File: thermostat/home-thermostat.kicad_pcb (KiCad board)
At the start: 2 copper layers, 92 parts, among them J1 Thermosthat, J2 Conn_01x24, J3 Conn_01x06, J4 AVR-ISP-6, Q1 BC817, Q2 BC817, Q3 BSS806NL6327, Q4 BC817, Q5 BSS806NL6327, Q6 BC817, Q7 BSS806NL6327, SW1 UP, SW2 DOWN, SW3 LEFT, SW4 RIGHT, SW5 OK, SW6 CANCEL, U1 ESP-12F, U2 MCP7940N-xMS, U3 LM2574M-5, U4 LD1117S33TR_SOT223, U5 AT24C512, U6 ATmega328P-AU, U7 LM358, U8 MCP9844, Y1 GEY KX-327NHT 12, Y2 20MHz ABM3B

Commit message: Started layouting thermosthat.
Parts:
- added Waveshare 4.2 Inch raw panel: waveshare_4.2_raw_panel, myfootprints:waveshare_4.2_raw_panel_folded_connector, B.Cu at (111.8, 135.9)
- moved C5 238.3 mm to (88.4, 168.9), turned to 270 degrees
- moved R4 223.3 mm to (86.6, 168.9), turned to 270 degrees
- moved U4 208.7 mm to (103.4, 102.9)
- moved C16 208.7 mm to (97.2, 105.2)
- moved C19 208.7 mm to (97.2, 102.9)
- moved U1 206.0 mm to (89.9, 156.7), turned to 90 degrees
- moved R3 203.4 mm to (90.4, 168.9), turned to 270 degrees
- moved C15 197.9 mm to (123.3, 119.5)
- moved C20 197.9 mm to (106.8, 110.4)
- moved D4 197.9 mm to (121.7, 111.9)
- moved L2 197.9 mm to (116.1, 110.4)
- moved U3 197.9 mm to (116.1, 119.3)
- moved R1 195.5 mm to (95.0, 144.8), turned to 270 degrees
- moved R5 189.2 mm to (98.0, 144.8), turned to 90 degrees
- moved C4 186.3 mm to (100.3, 169.2), turned to 270 degrees
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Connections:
- J3 pad 2: /DTR -> GND
- J3 pad 4: /RTC_INT -> /AVR_INT
- J3 pad 5: /AVR_INT -> /DTR
- J3 pad 6: GND -> /RTC_INT
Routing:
- net /GPIO0: track 0.00 -> 125.3 mm, vias 0 -> 2
- net GND: track 0.00 -> 87.8 mm, vias 0 -> 42
- net /GPIO15: track 0.00 -> 76.6 mm, vias 0 -> 2
- net /GPIO2: track 0.00 -> 76.1 mm, vias 0 -> 2
- net /SCK: track 0.00 -> 61.5 mm, vias 0 -> 2
- net /eink-RST: track 0.00 -> 61.3 mm, vias 0 -> 2
- net /MOSI: track 0.00 -> 58.1 mm, vias 0 -> 2
- net /SCL: track 0.00 -> 53.1 mm
- net /SDA: track 0.00 -> 50.5 mm
- net /nRST: track 0.00 -> 50.2 mm
- net +3V3: track 0.00 -> 33.2 mm, vias 0 -> 3
- net +5V: track 0.00 -> 30.1 mm, vias 0 -> 1
- net /PREVGL: track 0.00 -> 26.1 mm
- net /RESE: track 0.00 -> 24.6 mm
- net /PREVGH: track 0.00 -> 24.0 mm
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- added copper zone on B.Cu, net GND

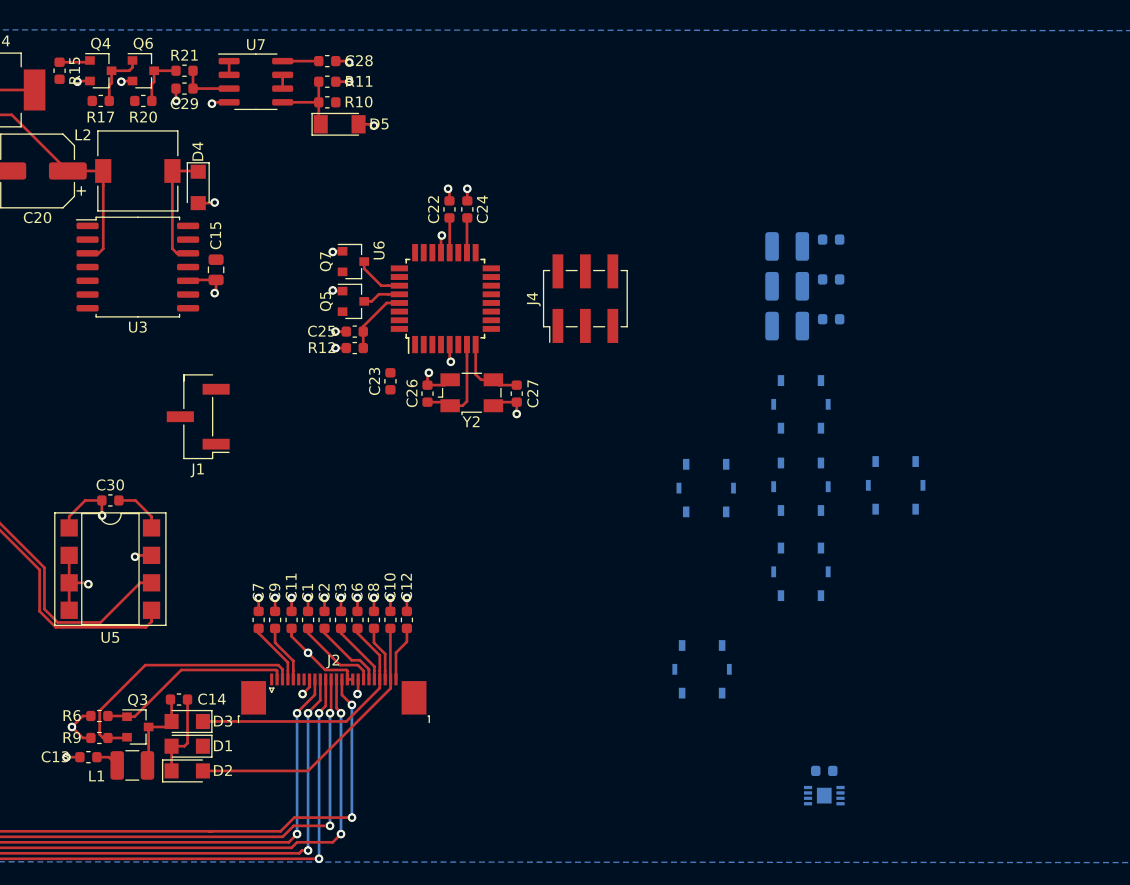
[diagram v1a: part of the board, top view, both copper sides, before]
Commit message: Advanced component placement, laid out some routes.
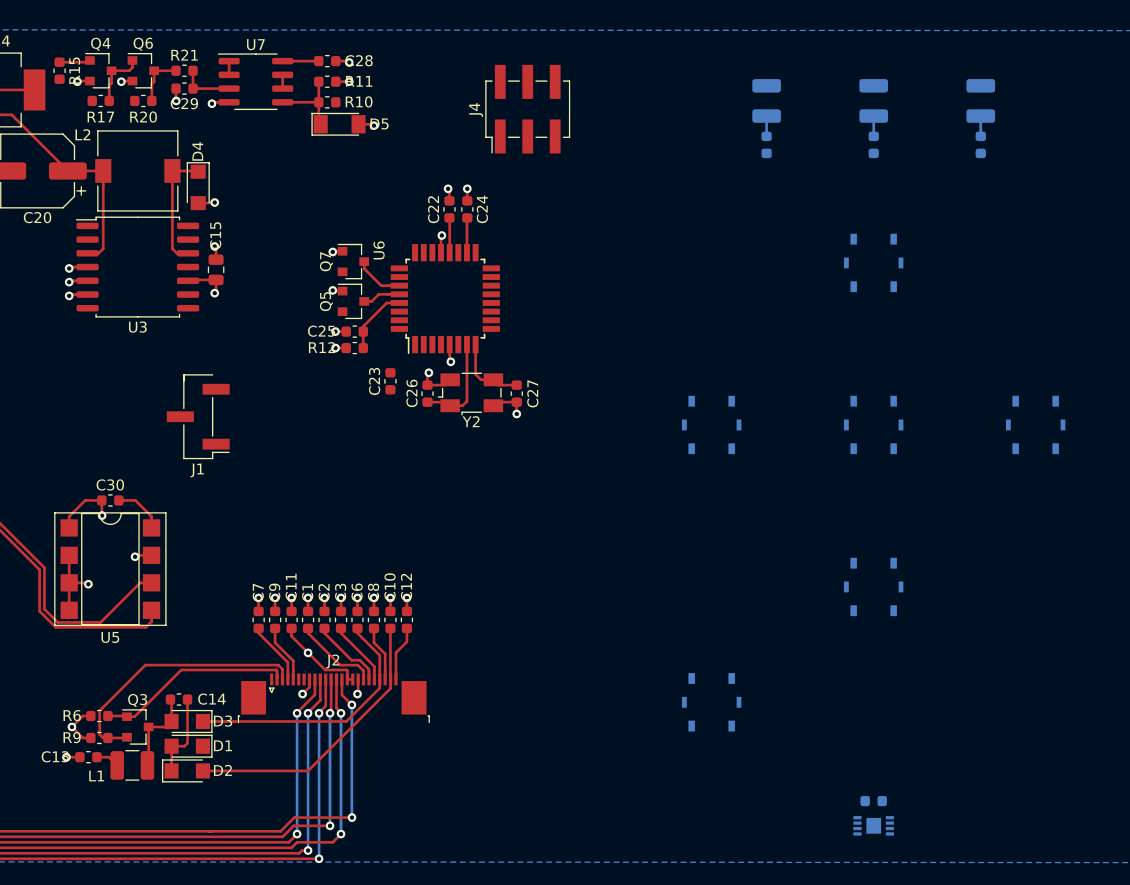
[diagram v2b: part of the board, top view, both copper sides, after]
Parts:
- moved D8 22.4 mm to (194.1, 103.9), turned to 270 degrees
- moved D7 20.9 mm to (174.2, 103.9), turned to 270 degrees
- moved D6 18.9 mm to (184.2, 103.9), turned to 270 degrees
- moved J4 18.3 mm to (152.1, 104.6)
- moved R14 17.2 mm to (174.2, 108.0), turned to 270 degrees
- moved R19 16.4 mm to (194.1, 108.0), turned to 270 degrees
- moved SW1 14.7 mm to (184.2, 118.9)
- moved SW3 14.1 mm to (199.1, 133.9)
- moved R13 13.1 mm to (184.2, 108.0), turned to 270 degrees
- moved SW5 8.83 mm to (184.2, 133.9)
- moved SW2 6.87 mm to (184.2, 148.8)
- moved SW4 5.86 mm to (169.2, 133.9)
- moved C21 5.36 mm to (184.2, 168.7)
- moved U8 5.36 mm to (184.2, 170.9)
- moved SW6 3.17 mm to (169.2, 159.5)
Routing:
- net GND: track 87.8 -> 94.4 mm, vias 42 -> 46
- net Net-(D8-Pad2): track 0.00 -> 1.88 mm
- net Net-(D7-Pad2): track 0.00 -> 1.88 mm
- net Net-(D6-Pad2): track 0.00 -> 1.88 mm

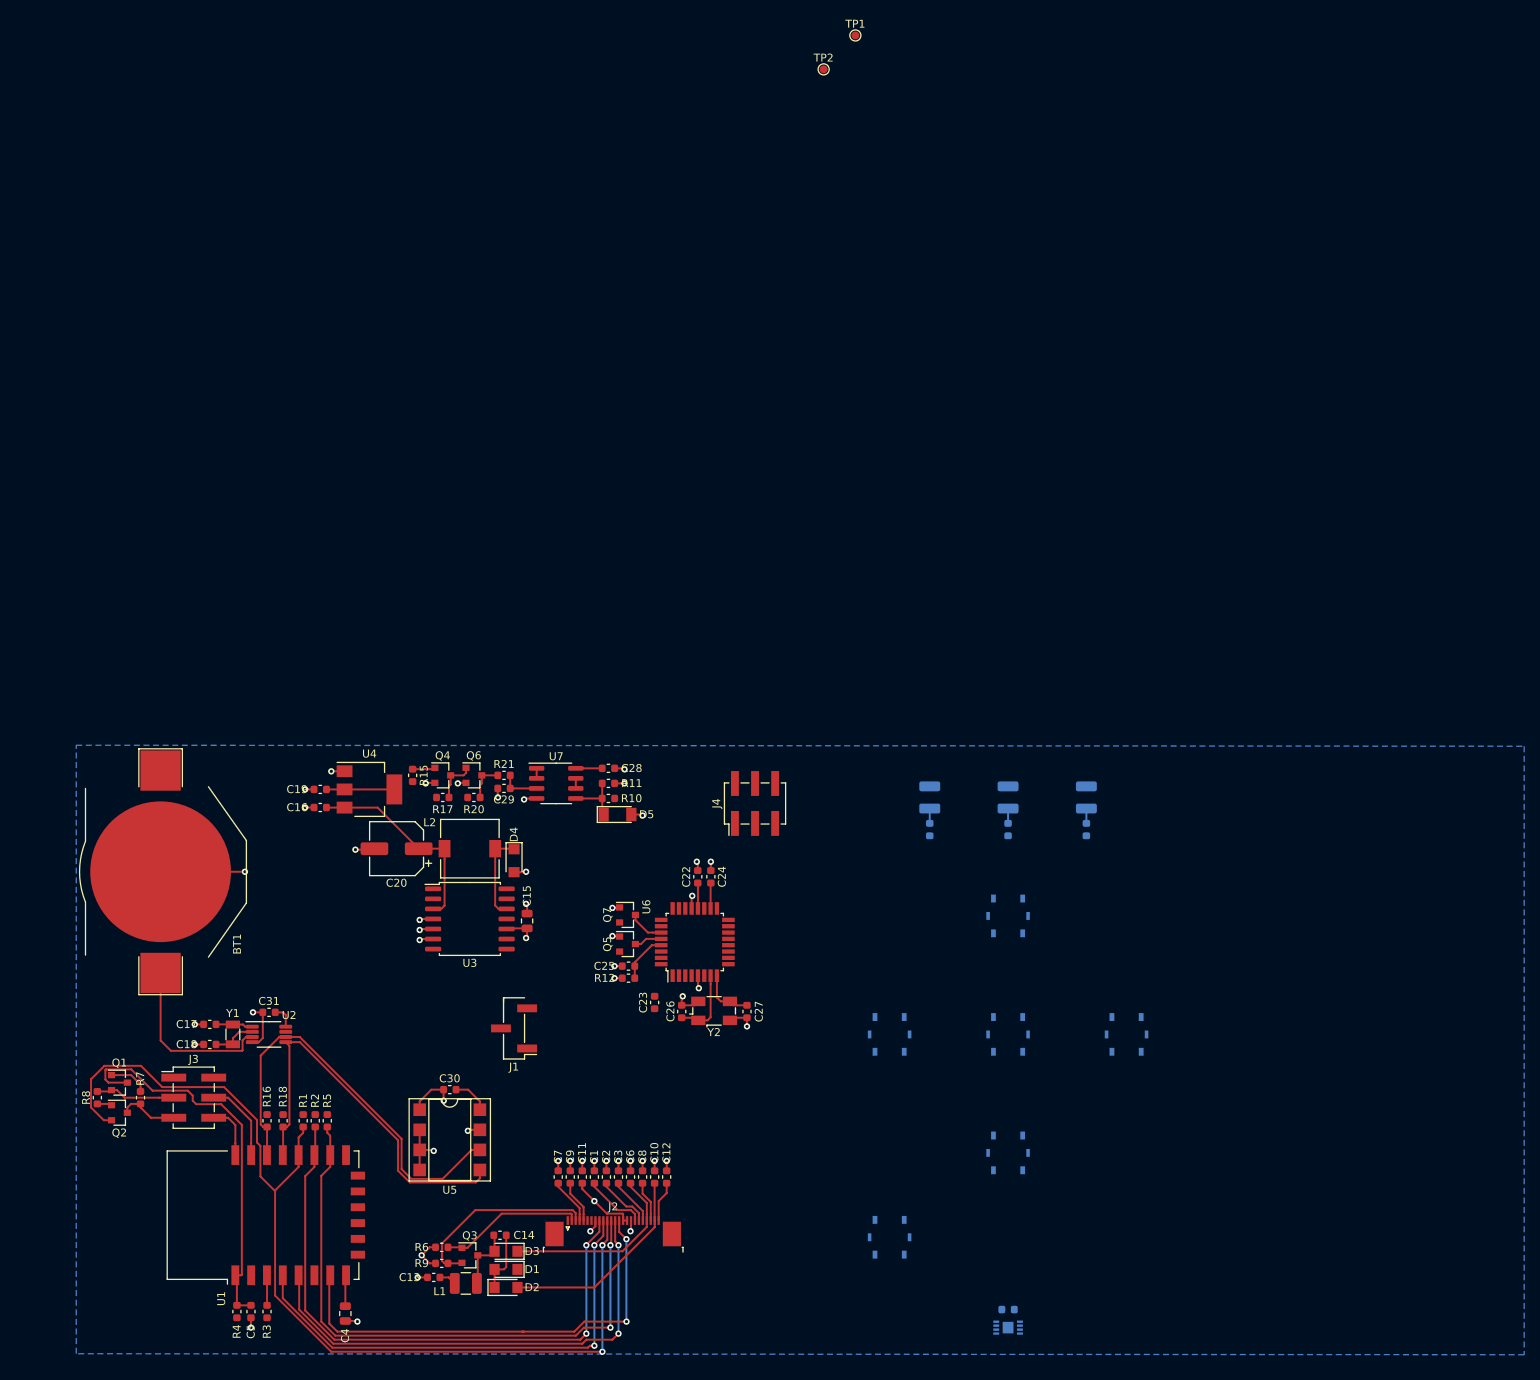
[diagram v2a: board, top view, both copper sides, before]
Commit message: Finished first PCB circuit draft. May not be optimal at all, regarding EMI etc.
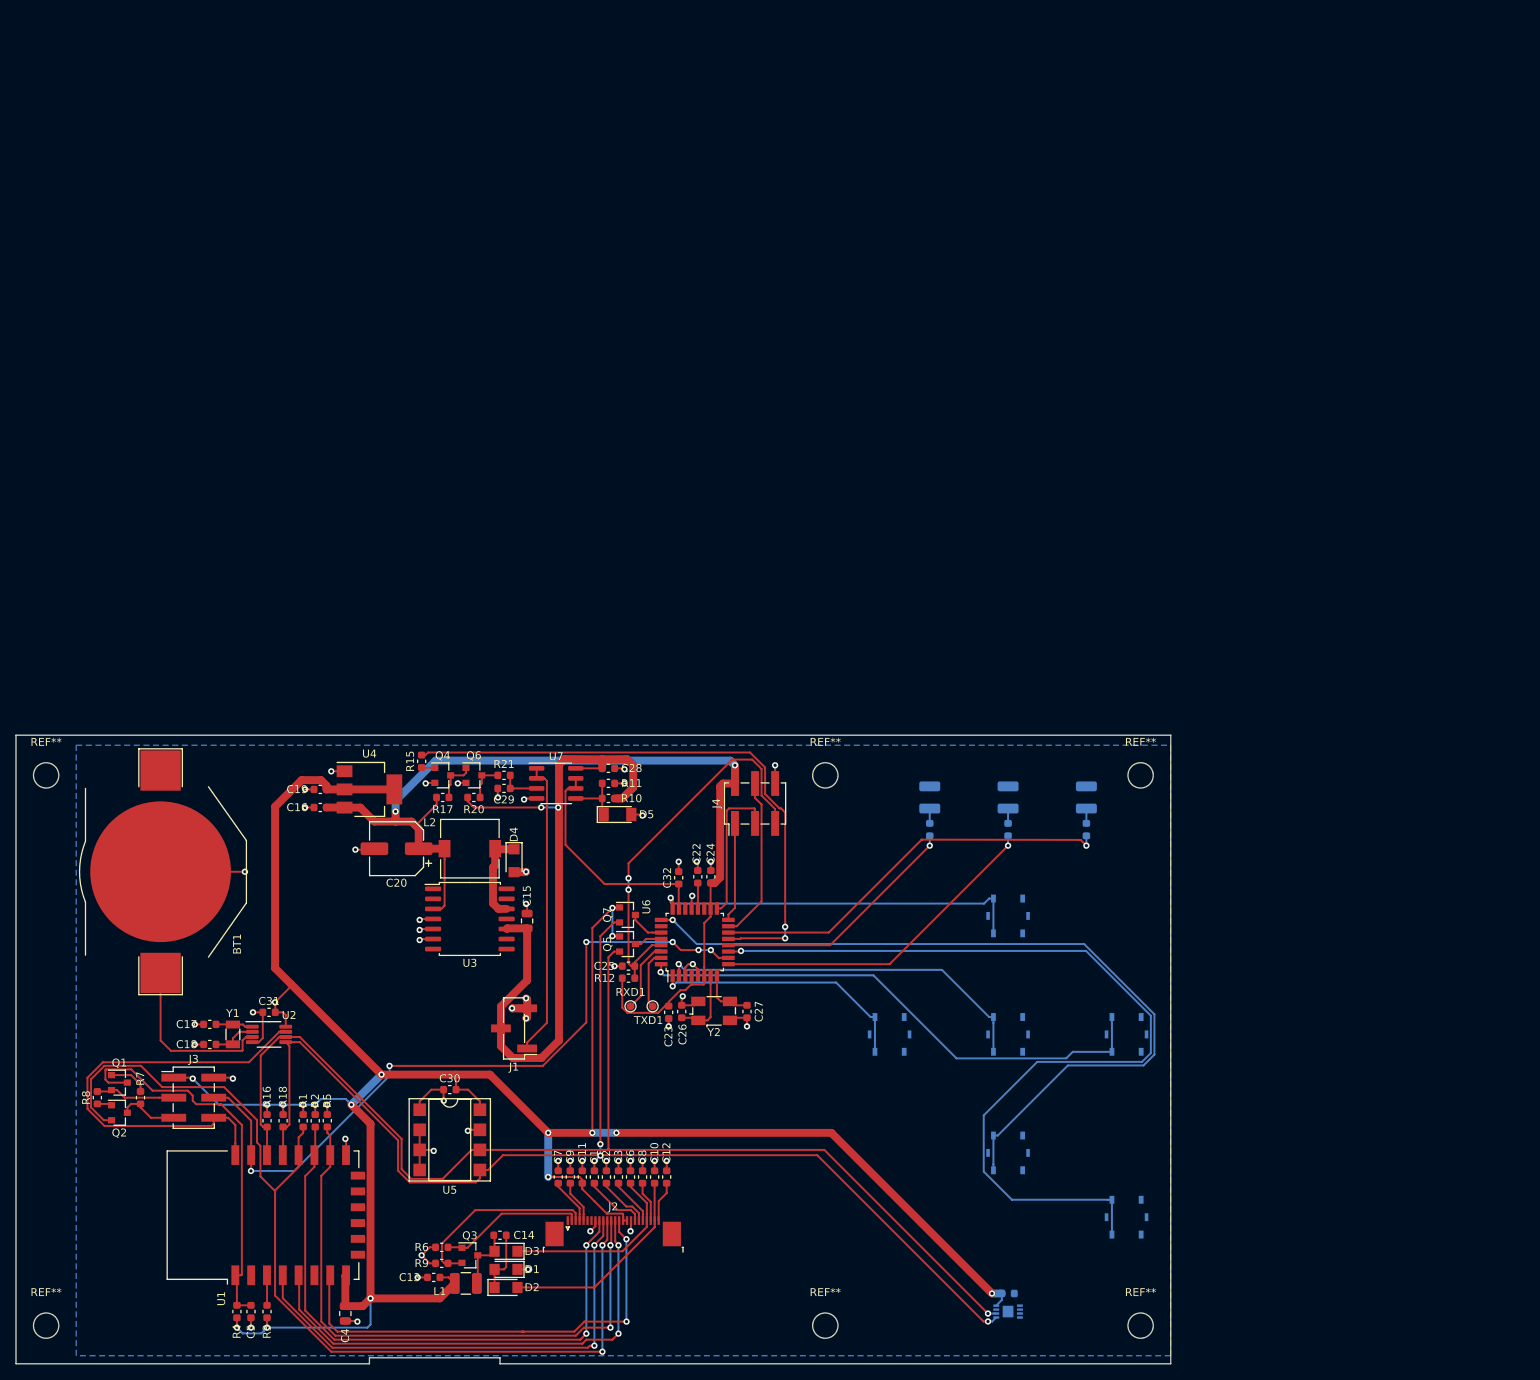
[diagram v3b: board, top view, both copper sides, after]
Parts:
- added C32: 10n, Capacitor_SMD:C_0603_1608Metric, F.Cu at (142.5, 114.0)
- added REF**: MountingHole_3.2mm_M3, MountingHole:MountingHole_3.2mm_M3, F.Cu at (62.5, 170.7)
- added REF**: MountingHole_3.2mm_M3, MountingHole:MountingHole_3.2mm_M3, F.Cu at (62.5, 101.1)
- added REF**: MountingHole_3.2mm_M3, MountingHole:MountingHole_3.2mm_M3, F.Cu at (200.9, 101.1)
- added REF**: MountingHole_3.2mm_M3, MountingHole:MountingHole_3.2mm_M3, F.Cu at (200.9, 170.7)
- added REF**: MountingHole_3.2mm_M3, MountingHole:MountingHole_3.2mm_M3, F.Cu at (161.0, 101.1)
- added REF**: MountingHole_3.2mm_M3, MountingHole:MountingHole_3.2mm_M3, F.Cu at (161.0, 170.7)
- RXD1: renamed from TP1; value TestPoint -> RXD
- TXD1: renamed from TP2; value TestPoint -> TXD
- moved RXD1 126.0 mm to (136.4, 130.3)
- moved TXD1 120.5 mm to (139.2, 130.3)
- moved SW6 30.1 mm to (199.1, 157.0)
- moved C23 2.17 mm to (141.2, 131.1)
- moved R15 2.11 mm to (110.0, 99.3), turned to 90 degrees
- moved C21 2.03 mm to (184.2, 166.6)
- moved U8 2.03 mm to (184.2, 168.9)
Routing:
- net +3V3: track 33.2 -> 321.8 mm, vias 3 -> 18
- net /regulator_out/CANCEL: track 0.00 -> 115.2 mm, vias 0 -> 1
- net /SDA: track 50.5 -> 156.5 mm, vias 0 -> 3
- net /regulator_out/DOWN: track 0.00 -> 101.4 mm, vias 0 -> 1
- net /SCL: track 53.1 -> 153.1 mm, vias 0 -> 1
- net +5V: track 30.1 -> 127.6 mm, vias 1 -> 2
- net +36V: track 7.24 -> 95.3 mm, vias 1 -> 2
- net /AVR_INT: track 10.3 -> 92.2 mm, vias 0 -> 6
- net /regulator_out/pwm_sig: track 0.00 -> 74.3 mm, vias 0 -> 2
- net /regulator_out/LEFT: track 0.00 -> 67.4 mm, vias 0 -> 1
- net /regulator_out/LED_GREEN: track 0.00 -> 51.7 mm, vias 0 -> 1
- net /RTC_INT: track 6.92 -> 56.1 mm
- net /regulator_out/OK: track 0.00 -> 48.4 mm, vias 0 -> 1
- net /regulator_out/UP: track 0.00 -> 47.6 mm, vias 0 -> 1
- net /regulator_out/avr_rst: track 6.24 -> 50.2 mm, vias 0 -> 2
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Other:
- board outline added: 146 x 79.5 mm
